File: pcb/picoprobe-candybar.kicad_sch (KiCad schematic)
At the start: 25 parts, among them J1 PinHeader_2x04, J2 SWD-UART_PicoprobeCandybar, Q1 BSS806N, SW1 SW-R1-1A-E-1-0, SW2 SLW-156646-5A-N-D, U1 74AUP1T17, U2 74AUP1T17

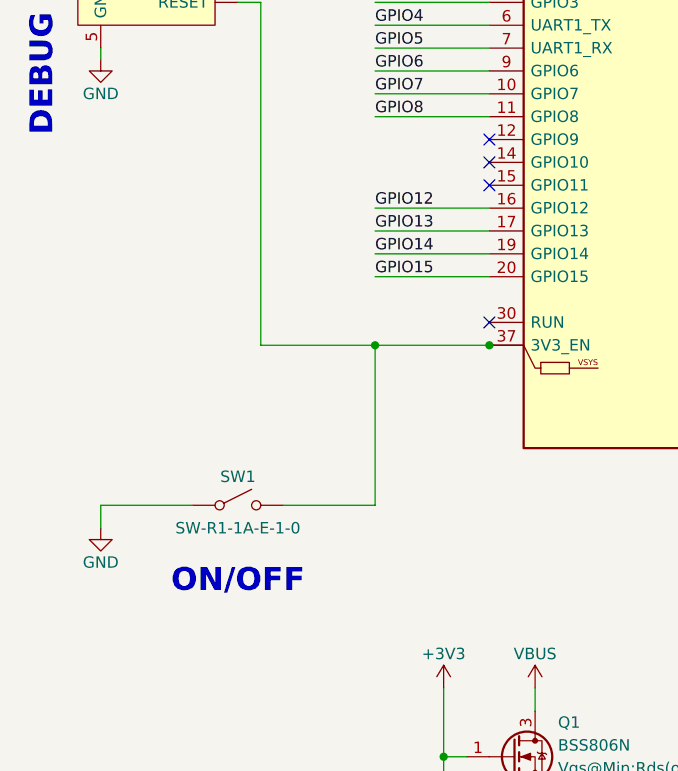
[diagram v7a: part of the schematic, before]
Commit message: Add debounce RC filter to on/off switch
3V3_EN has a 100k pull-up.
RT6150B-33GQW registers 0.4V as logic-low (off).
Debounce resistor will create voltage divider:

  Vout > (Rl * Vcc) / (Rl + Rh)
  0.4V > (Rl * 5V) / (Rl + 100k)
  Rl < 8696

Voltage at divider for Rl of 470ohm:

  Vout = Rl * Vcc / (Rl + Rh)
  Vout = 470 * 5V / (470 + 100k)
  Vout = 0.023V

RT6150B-33GQW registers 1.2V as logic-high (on).
Capacitance for >1ms DISCHARGE (on) debounce time:

  Vc < Vs * (e ^ (-t / (R * C)))
  (5V - 1.2V) < (5V - 0.023V) * (e ^ (-1ms / (100k * C)))
  C > 37.1nF

Selected:

  R: 470
  C: 0.1uF

  (Both are values which already exist in schematic/BOM)

Which results in a discharge (on) time of:

  Vc < Vs * (e ^ (-t / (R * C)))
  (5V - 1.2V) = (5V - 0.023V) * (e ^ (-t / (100k * 0.1uF)))
  t(on) = 2.7ms

Power off (charge) will not be as graceful:

  Vc < Vs * (1 - e ^ (-t / (R * C)))
  (5V - 0.4V) = (5V - 0.023V) * (1 - e ^ (-t / (470 * 0.1uF)))
  t(off) = 121us

But it's probably still sufficient at filtering bounces,
and graceful shutdown is not as important as startup.

<https://datasheets.raspberrypi.com/pico/pico-datasheet.pdf>
<https://www.richtek.com/assets/product_file/RT6150A=RT6150B/DS6150AB-05.pdf>
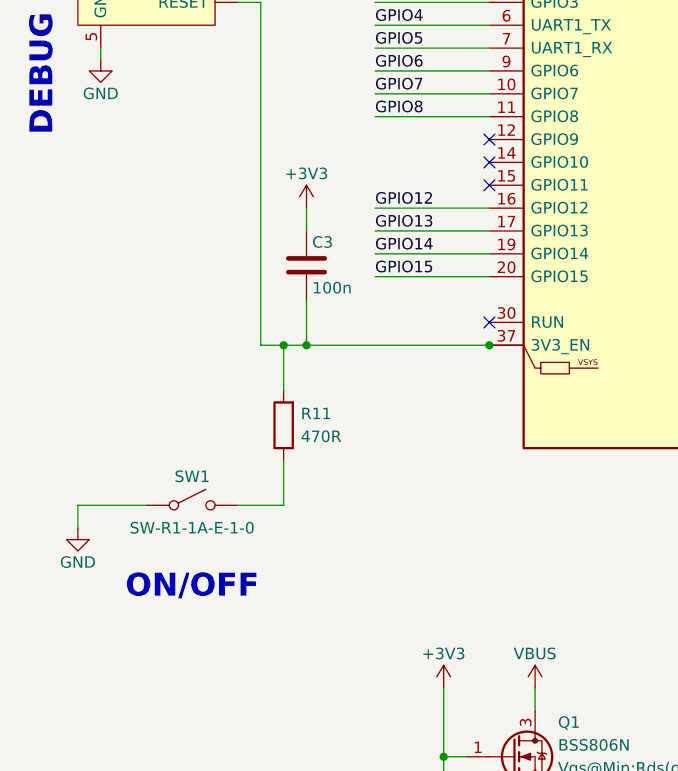
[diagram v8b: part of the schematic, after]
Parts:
- added C3: 100n, symbol Device:C
- added R11: 470R, symbol Device:R
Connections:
- net +3V3: now also C3.1
- net at A1.37 (3V3_EN), J2.4 (~{RESET}): now also C3.2, R11.2; no longer SW1.2 (B)
- new net: R11.1, SW1.2 (B)
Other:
- moved on the sheet: SW1
